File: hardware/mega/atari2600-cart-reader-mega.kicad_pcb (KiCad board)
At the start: 2 copper layers, 101.6 x 53.3 mm, 4 parts, among them J1 Atari 2600 Cartridge-Slot

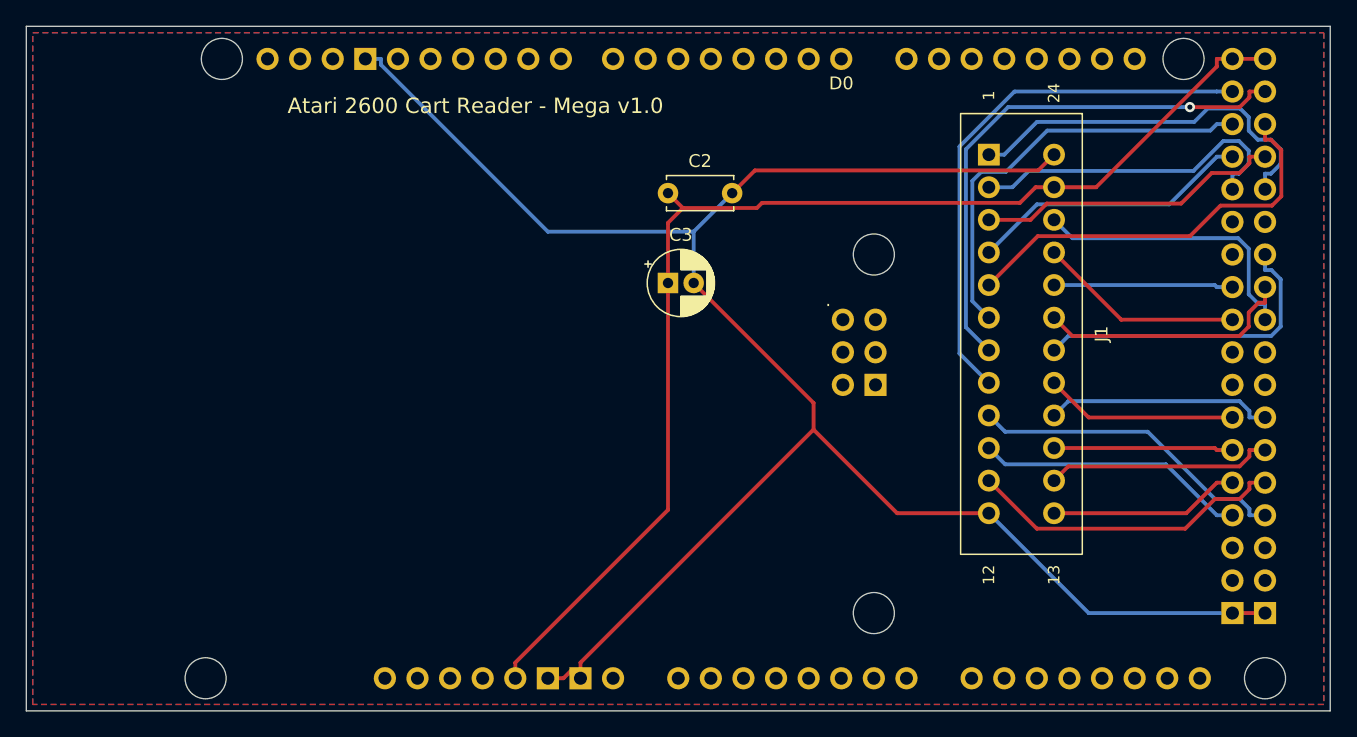
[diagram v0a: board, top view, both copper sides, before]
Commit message: Set cartridge slot row spacing to measured 5.5 mm
Stefan measured 6 mm across the outer pin edges with 0.5 mm pins.
Both shields re-routed; DRC 0 errors, 0 unconnected.

Co-Authored-By: Claude Opus 5.5 (1M context) <noreply@anthropic.com>
Claude-Session: https://claude.ai/code/session_015VQCpzuZ22TPQEmx9cLrbH
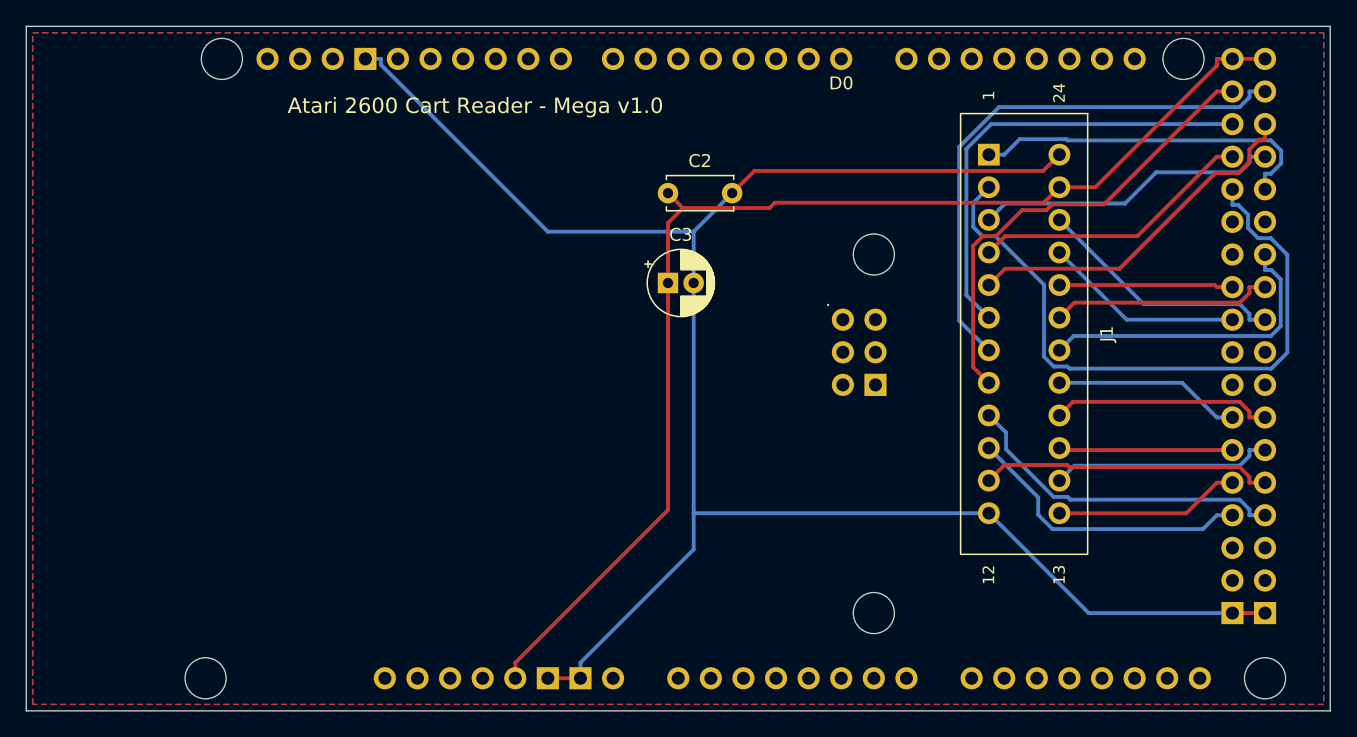
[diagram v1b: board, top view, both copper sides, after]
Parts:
- J1: footprint atari:Atari2600_Cart_Slot_2x12_P2.54mm_Row5.08mm -> atari:Atari2600_Cart_Slot_2x12_P2.54mm_Row5.50mm
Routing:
- net /A6: track 25.9 -> 51.8 mm
- net /A0: track 42.4 -> 36.4 mm
- net /A3: track 32.1 -> 28.0 mm
- net /A8: track 22.5 -> 19.5 mm
- net /A10: track 20.0 -> 17.3 mm
- net /A7: track 30.1 -> 27.4 mm
- net /A2: track 33.3 -> 35.4 mm
- net /D2: track 24.8 -> 22.9 mm
- net /D1: track 21.2 -> 22.8 mm
- net GND: track 152.1 -> 151.1 mm
- net /A1: track 41.8 -> 42.7 mm, vias 1 -> 0
- net /D0: track 25.0 -> 25.8 mm

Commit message: Switched cartridge supply, Nano board, guide mounting holes
- BC327 high-side switch with 200 mA polyfuse and rail sense on all boards
- Firmware powers the cartridge only after an orientation check
  (experimental thresholds, S command for calibration)
- New carrier board for a plugged-in Arduino Nano (same circuit and
  firmware as the Uno)
- Slot footprint with M2.5 flange holes and the guide base plate outline;
  build checks that the plate area stays free
- ICSP header removed from the shields, Uno hole next to it removed,
  Mega slot moved to the board centre
- Fix: struct Scheme declared before Arduino's generated prototypes
  (the sketch did not compile before)
- Switch schematic and prototype photos

Co-Authored-By: Claude Opus 5.5 (1M context) <noreply@anthropic.com>
Claude-Session: https://claude.ai/code/session_015VQCpzuZ22TPQEmx9cLrbH
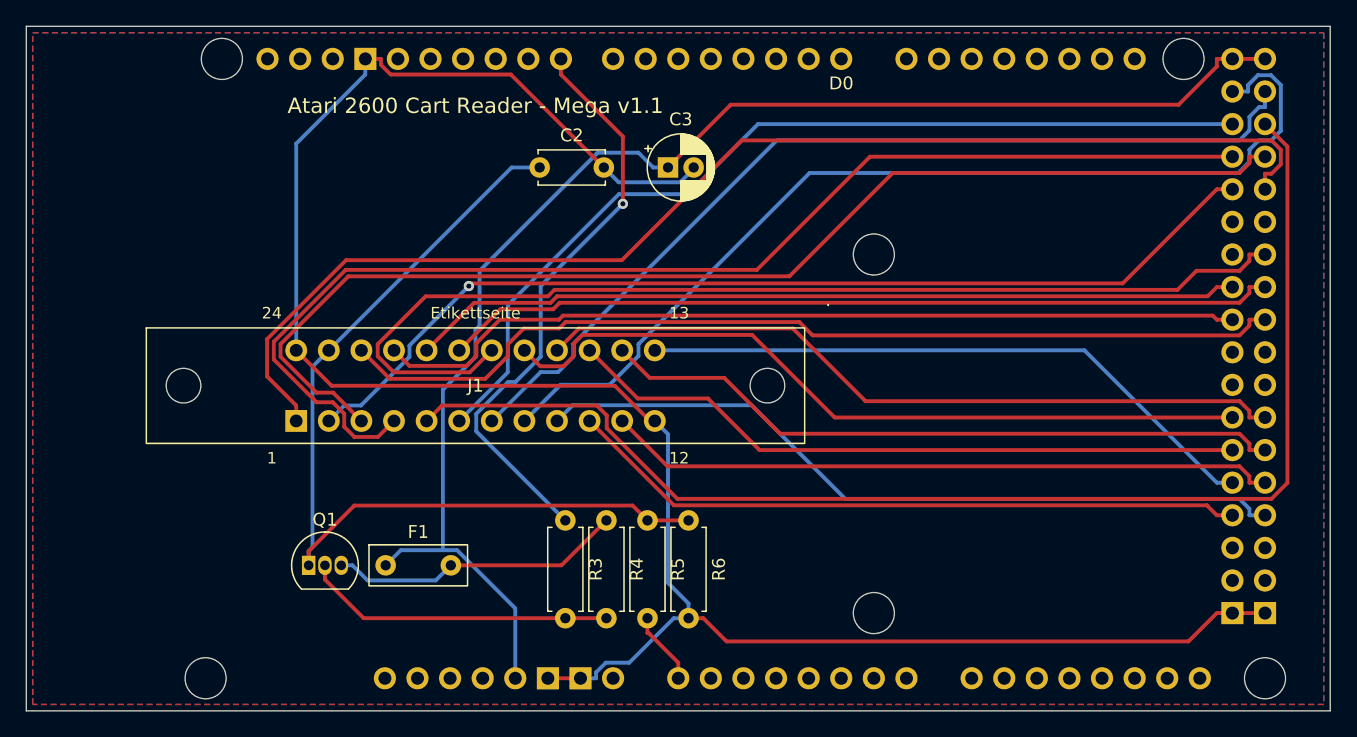
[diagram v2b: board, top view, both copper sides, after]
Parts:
- added F1: MF-R020 (200 mA), atari:Fuse_PTC_Radial_P5.08mm, F.Cu at (128.0, 142.0)
- added Q1: BC327, Package_TO_SOT_THT:TO-92_Inline, F.Cu at (122.0, 142.0)
- added R3: 1k, Resistor_THT:R_Axial_DIN0207_L6.3mm_D2.5mm_P7.62mm_Horizontal, F.Cu at (142.0, 138.5)
- added R4: 10k, Resistor_THT:R_Axial_DIN0207_L6.3mm_D2.5mm_P7.62mm_Horizontal, F.Cu at (145.2, 138.5)
- added R5: 10k, Resistor_THT:R_Axial_DIN0207_L6.3mm_D2.5mm_P7.62mm_Horizontal, F.Cu at (148.4, 138.5)
- added R6: 100k, Resistor_THT:R_Axial_DIN0207_L6.3mm_D2.5mm_P7.62mm_Horizontal, F.Cu at (151.6, 138.5)
- J1: footprint atari:Atari2600_Cart_Slot_2x12_P2.54mm_Row5.50mm -> atari:Atari2600_Cart_Slot_2x12_P2.54mm_Row5.50mm_Guide
- moved J1 57.8 mm to (121.0, 130.8), turned to 0 degrees
- moved C2 10.2 mm to (140.0, 111.0)
- moved C3 9.00 mm to (150.0, 111.0)
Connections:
- A1 pad A0: (no net) -> /CART_SENSE
- A1 pad D8: (no net) -> /CART_PWR
- C2 pad 1: +5V -> /CART_5V
- J1 pad 23: +5V -> /CART_5V
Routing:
- net /A4: track 22.1 -> 95.0 mm
- net /CART_5V: track 0.00 -> 72.4 mm
- net /A3: track 28.0 -> 100.4 mm
- net /A7: track 27.4 -> 96.9 mm
- net /A5: track 23.8 -> 92.4 mm
- net /A12: track 24.4 -> 83.4 mm
- net /A8: track 19.5 -> 74.9 mm
- net /A9: track 15.7 -> 68.2 mm
- net /A11: track 13.5 -> 64.8 mm
- net /A10: track 17.3 -> 65.1 mm
- net /CART_PWR: track 0.00 -> 45.9 mm, vias 0 -> 1
- net /D7: track 14.6 -> 59.9 mm
- net /D6: track 17.2 -> 59.0 mm
- net /A0: track 36.4 -> 77.9 mm
- net /D5: track 13.5 -> 53.3 mm
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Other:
- board text added: "Atari 2600 Cart Reader - Mega v1.1"
- board text removed: "Atari 2600 Cart Reader - Mega v1.0"

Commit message: Silkscreen: reference and value per part, fambach.net on the front
labels.py adds the silkscreen texts after routing, so the copper stays unchanged.

Co-Authored-By: Claude Opus 5.5 <noreply@anthropic.com>
Claude-Session: https://claude.ai/code/session_015VQCpzuZ22TPQEmx9cLrbH
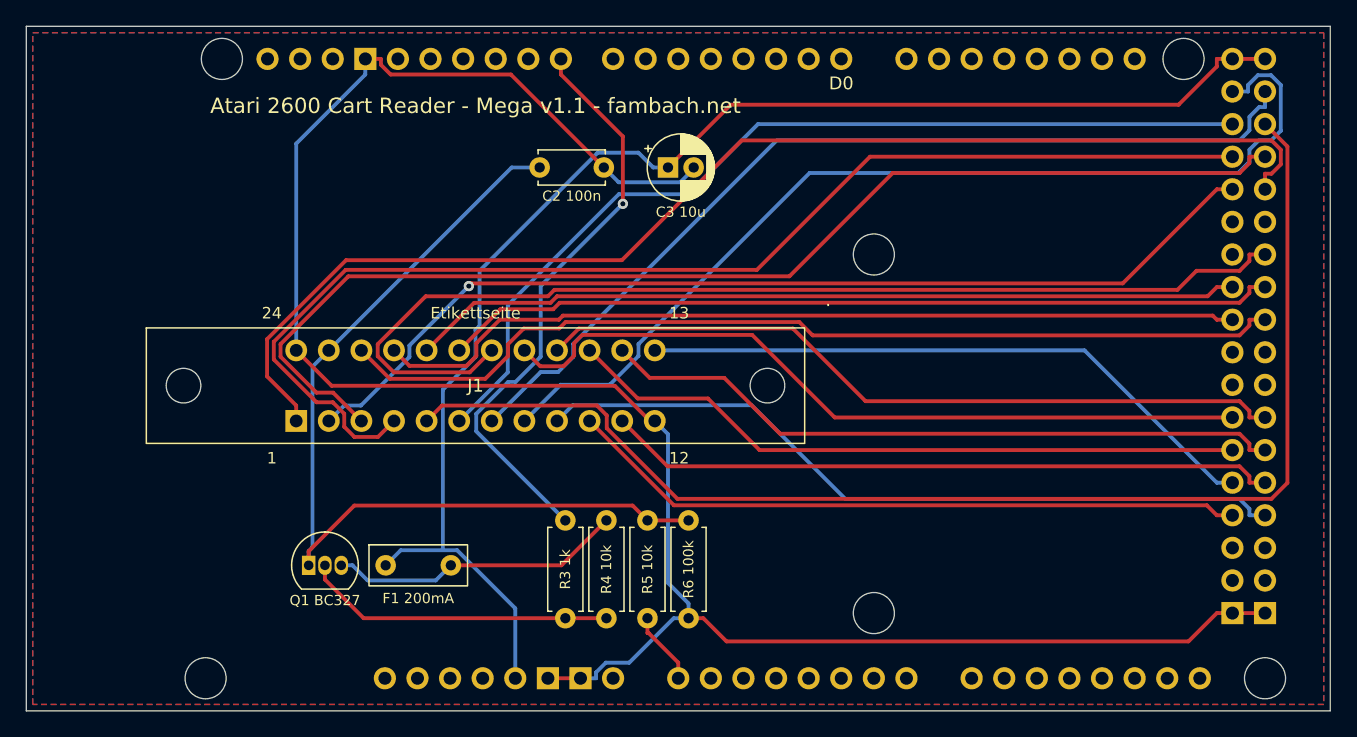
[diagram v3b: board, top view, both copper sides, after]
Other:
- board text added: "Atari 2600 Cart Reader - Mega v1.1 - fambach.net"
- board text added: "C2 100n"
- board text added: "C3 10u"
- board text added: "F1 200mA"
- board text added: "Q1 BC327"
- board text added: "R3 1k"
- board text added: "R4 10k"
- board text added: "R5 10k"
- board text added: "R6 100k"
- board text removed: "Atari 2600 Cart Reader - Mega v1.1"
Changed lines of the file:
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@@
     (tags "Resistor Axial_DIN0207 series Axial Horizontal pin pitch 7.62mm 0.25W = 1/4W length 6.3mm diameter 2.5mm")
     (attr through_hole)
-    (fp_text reference "R4" (at 3.81 -2.37 -90) (layer "F.SilkS")
+    (fp_text reference "R4" (at 3.81 -2.37 -90) (layer "F.SilkS") hide
         (effects (font (size 1 1) (thickness 0.15)))
     )
@@
     (tags "Resistor Axial_DIN0207 series Axial Horizontal pin pitch 7.62mm 0.25W = 1/4W length 6.3mm diameter 2.5mm")
     (attr through_hole)
-    (fp_text reference "R5" (at 3.81 -2.37 -90) (layer "F.SilkS")
+    (fp_text reference "R5" (at 3.81 -2.37 -90) (layer "F.SilkS") hide
         (effects (font (size 1 1) (thickness 0.15)))
     )
@@
     (tags "CP Radial series Radial pin pitch 2.00mm  diameter 5mm Electrolytic Capacitor")
     (attr through_hole)
-    (fp_text reference "C3" (at 1 -3.75) (layer "F.SilkS")
+    (fp_text reference "C3" (at 1 -3.75) (layer "F.SilkS") hide
         (effects (font (size 1 1) (thickness 0.15)))
     )
@@
     (tags "C Disc series Radial pin pitch 5.00mm  diameter 5mm width 2.5mm Capacitor")
     (attr through_hole)
-    (fp_text reference "C2" (at 2.5 -2.5) (layer "F.SilkS")
+    (fp_text reference "C2" (at 2.5 -2.5) (layer "F.SilkS") hide
         (effects (font (size 1 1) (thickness 0.15)))
     )
@@
     (tags "to-92 sc-43 sc-43a sot54 PA33 transistor")
     (attr through_hole)
-    (fp_text reference "Q1" (at 1.27 -3.56) (layer "F.SilkS")
+    (fp_text reference "Q1" (at 1.27 -3.56) (layer "F.SilkS") hide
         (effects (font (size 1 1) (thickness 0.15)))
     )
@@
     (tags "polyfuse PTC radial")
     (attr through_hole)
-    (fp_text reference "F1" (at 2.54 -2.6) (layer "F.SilkS")
+    (fp_text reference "F1" (at 2.54 -2.6) (layer "F.SilkS") hide
         (effects (font (size 1 1) (thickness 0.15)))
     )
@@
     (tags "Resistor Axial_DIN0207 series Axial Horizontal pin pitch 7.62mm 0.25W = 1/4W length 6.3mm diameter 2.5mm")
     (attr through_hole)
-    (fp_text reference "R6" (at 3.81 -2.37 -90) (layer "F.SilkS")
+    (fp_text reference "R6" (at 3.81 -2.37 -90) (layer "F.SilkS") hide
         (effects (font (size 1 1) (thickness 0.15)))
     )
@@
     (tags "Resistor Axial_DIN0207 series Axial Horizontal pin pitch 7.62mm 0.25W = 1/4W length 6.3mm diameter 2.5mm")
     (attr through_hole)
-    (fp_text reference "R3" (at 3.81 -2.37 -90) (layer "F.SilkS")
+    (fp_text reference "R3" (at 3.81 -2.37 -90) (layer "F.SilkS") hide
         (effects (font (size 1 1) (thickness 0.15)))
     )
@@
   (gr_line (start 201.6 153.34) (end 100 153.34)
     (stroke (width 0.1) (type default)) (layer "Edge.Cuts"))
+  (gr_text "fambach.net" (at 122 128) (layer "B.SilkS")
+    (effects (font (size 1 1) (thickness 0.15)) (justify mirror))
+  )
   (gr_text "github.com/sfambach/arduino-atari2600-cart-reader" (at 122 130) (layer "B.SilkS")
     (effects (font (size 0.8 0.8) (thickness 0.12)) (justify mirror))
   )
-  (gr_text "fambach.net" (at 122 128) (layer "B.SilkS")
-    (effects (font (size 1 1) (thickness 0.15)) (justify mirror))
-  )
-  (gr_text "Atari 2600 Cart Reader - Mega v1.1" (at 135 106.2) (layer "F.SilkS")
+  (gr_text "R6 100k" (at 151.599999 142.31 90) (layer "F.SilkS")
+    (effects (font (size 0.8 0.8) (thickness 0.12)))
+  )
+  (gr_text "R4 10k" (at 145.199999 142.31 90) (layer "F.SilkS")
+    (effects (font (size 0.8 0.8) (thickness 0.12)))
+  )
+  (gr_text "C3 10u" (at 151 114.475) (layer "F.SilkS")
+    (effects (font (size 0.8 0.8) (thickness 0.12)))
+  )
+  (gr_text "F1 200mA" (at 130.54 144.575) (layer "F.SilkS")
+    (effects (font (size 0.8 0.8) (thickness 0.12)))
+  )
+  (gr_text "R3 1k" (at 142 142.31 90) (layer "F.SilkS")
+    (effects (font (size 0.8 0.8) (thickness 0.12)))
+  )
+  (gr_text "R5 10k" (at 148.4 142.31 90) (layer "F.SilkS")
+    (effects (font (size 0.8 0.8) (thickness 0.12)))
+  )
+  (gr_text "Q1 BC327" (at 123.27 144.735) (layer "F.SilkS")
+    (effects (font (size 0.8 0.8) (thickness 0.12)))
+  )
+  (gr_text "Atari 2600 Cart Reader - Mega v1.1 - fambach.net" (at 135 106.2) (layer "F.SilkS")
     (effects (font (size 1.2 1.2) (thickness 0.18)))
   )
+  (gr_text "C2 100n" (at 142.5 113.225) (layer "F.SilkS")
+    (effects (font (size 0.8 0.8) (thickness 0.12)))
+  )
   (segment (start 192.7645 102.54) (end 192.7645 103.1327) (width 0.3) (layer "F.Cu") (net 1))

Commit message: Reset and read buttons on all boards (v1.2)
SW1 resets the Arduino, SW2 on A1 repeats the last dump; dump.py listen saves button dumps.

Co-Authored-By: Claude Opus 5.5 <noreply@anthropic.com>
Claude-Session: https://claude.ai/code/session_015VQCpzuZ22TPQEmx9cLrbH
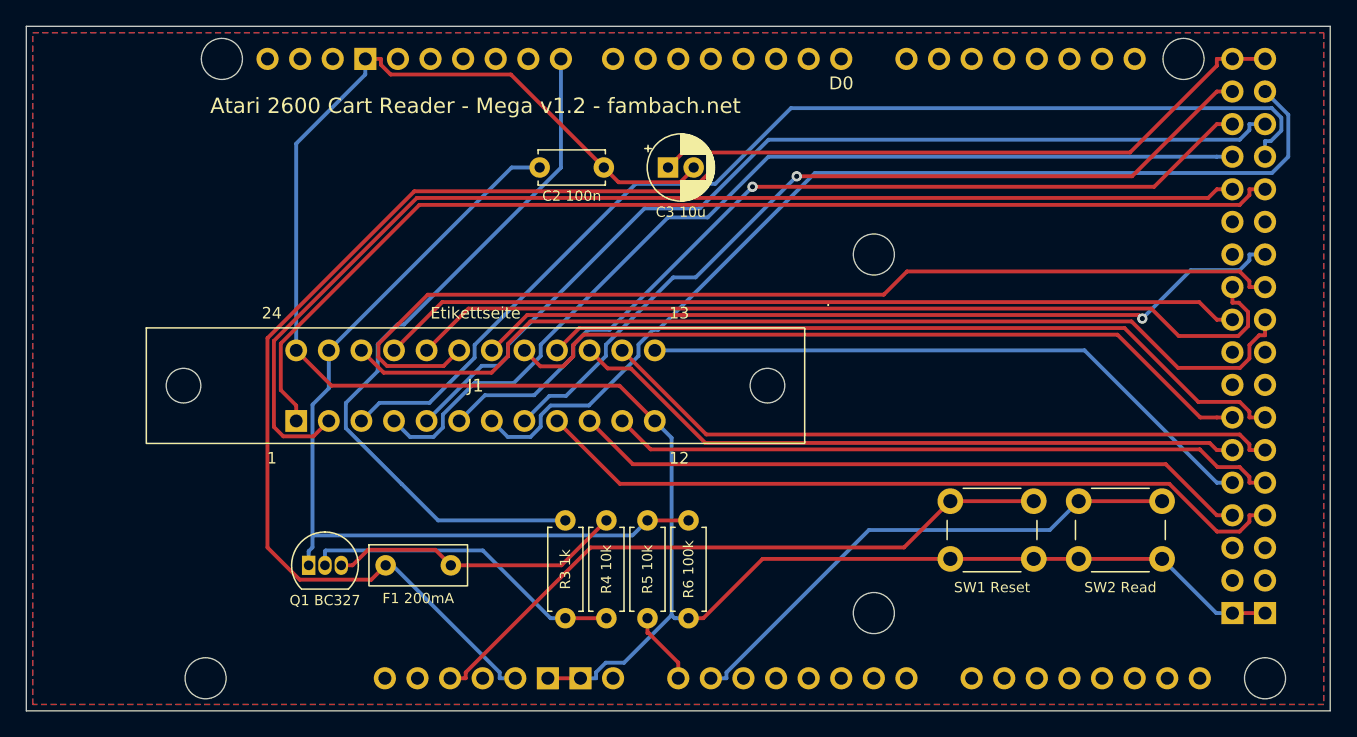
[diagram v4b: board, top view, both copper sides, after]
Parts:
- added SW1: Reset, Button_Switch_THT:SW_PUSH_6mm, F.Cu at (172.0, 137.0)
- added SW2: Read, Button_Switch_THT:SW_PUSH_6mm, F.Cu at (182.0, 137.0)
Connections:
- A1 pad A1: (no net) -> /READ
- A1 pad RST1: (no net) -> /RESET
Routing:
- net /RESET: track 0.00 -> 51.5 mm
- net /READ: track 0.00 -> 41.1 mm
- net /A3: track 100.4 -> 75.7 mm
- net +5V: track 110.2 -> 132.7 mm
- net /A12: track 83.4 -> 63.8 mm, vias 0 -> 1
- net /A4: track 95.0 -> 76.0 mm
- net /A10: track 65.1 -> 80.3 mm
- net /A6: track 78.4 -> 91.4 mm, vias 1 -> 0
- net /A0: track 77.9 -> 66.3 mm, vias 0 -> 1
- net /CART_PWR: track 45.9 -> 56.1 mm, vias 1 -> 0
- net /A7: track 96.9 -> 88.5 mm
- net /A5: track 92.4 -> 86.5 mm
- net /A1: track 72.8 -> 78.5 mm
- net /A11: track 64.8 -> 70.4 mm
- net /CART_5V: track 72.4 -> 69.5 mm
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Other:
- board text added: "Atari 2600 Cart Reader - Mega v1.2 - fambach.net"
- board text added: "SW1 Reset"
- board text added: "SW2 Read"
- board text removed: "Atari 2600 Cart Reader - Mega v1.1 - fambach.net"
